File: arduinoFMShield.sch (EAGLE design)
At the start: 32 parts, among them IC1 ATMEGA168-MU, IC2 FT232RQ, X1 MINI-USB-32005-301, X2 R141426

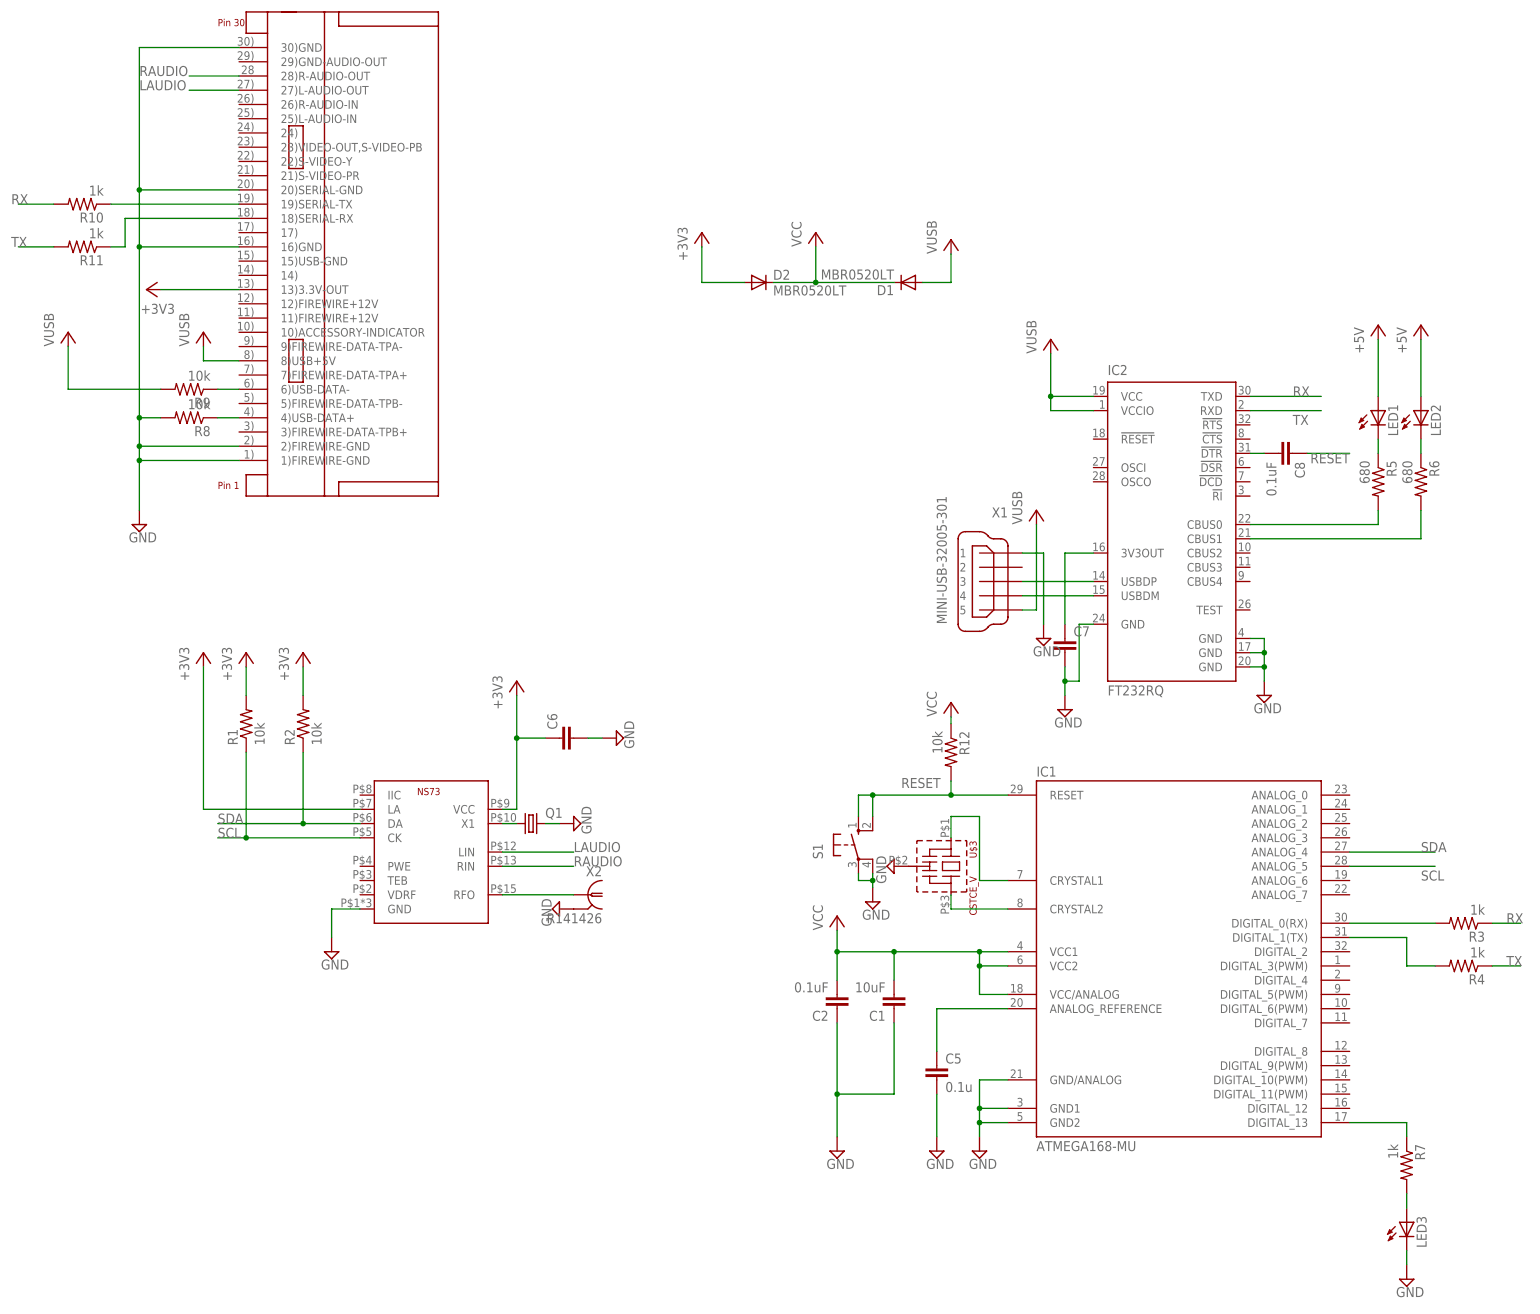
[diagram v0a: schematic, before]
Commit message: 8/31/2013 Changed FTDI chip and atmega to bigger package for easier soldering. Add murata resonator
Signed-off-by: goose1987 <phamh1987@gmail.com>
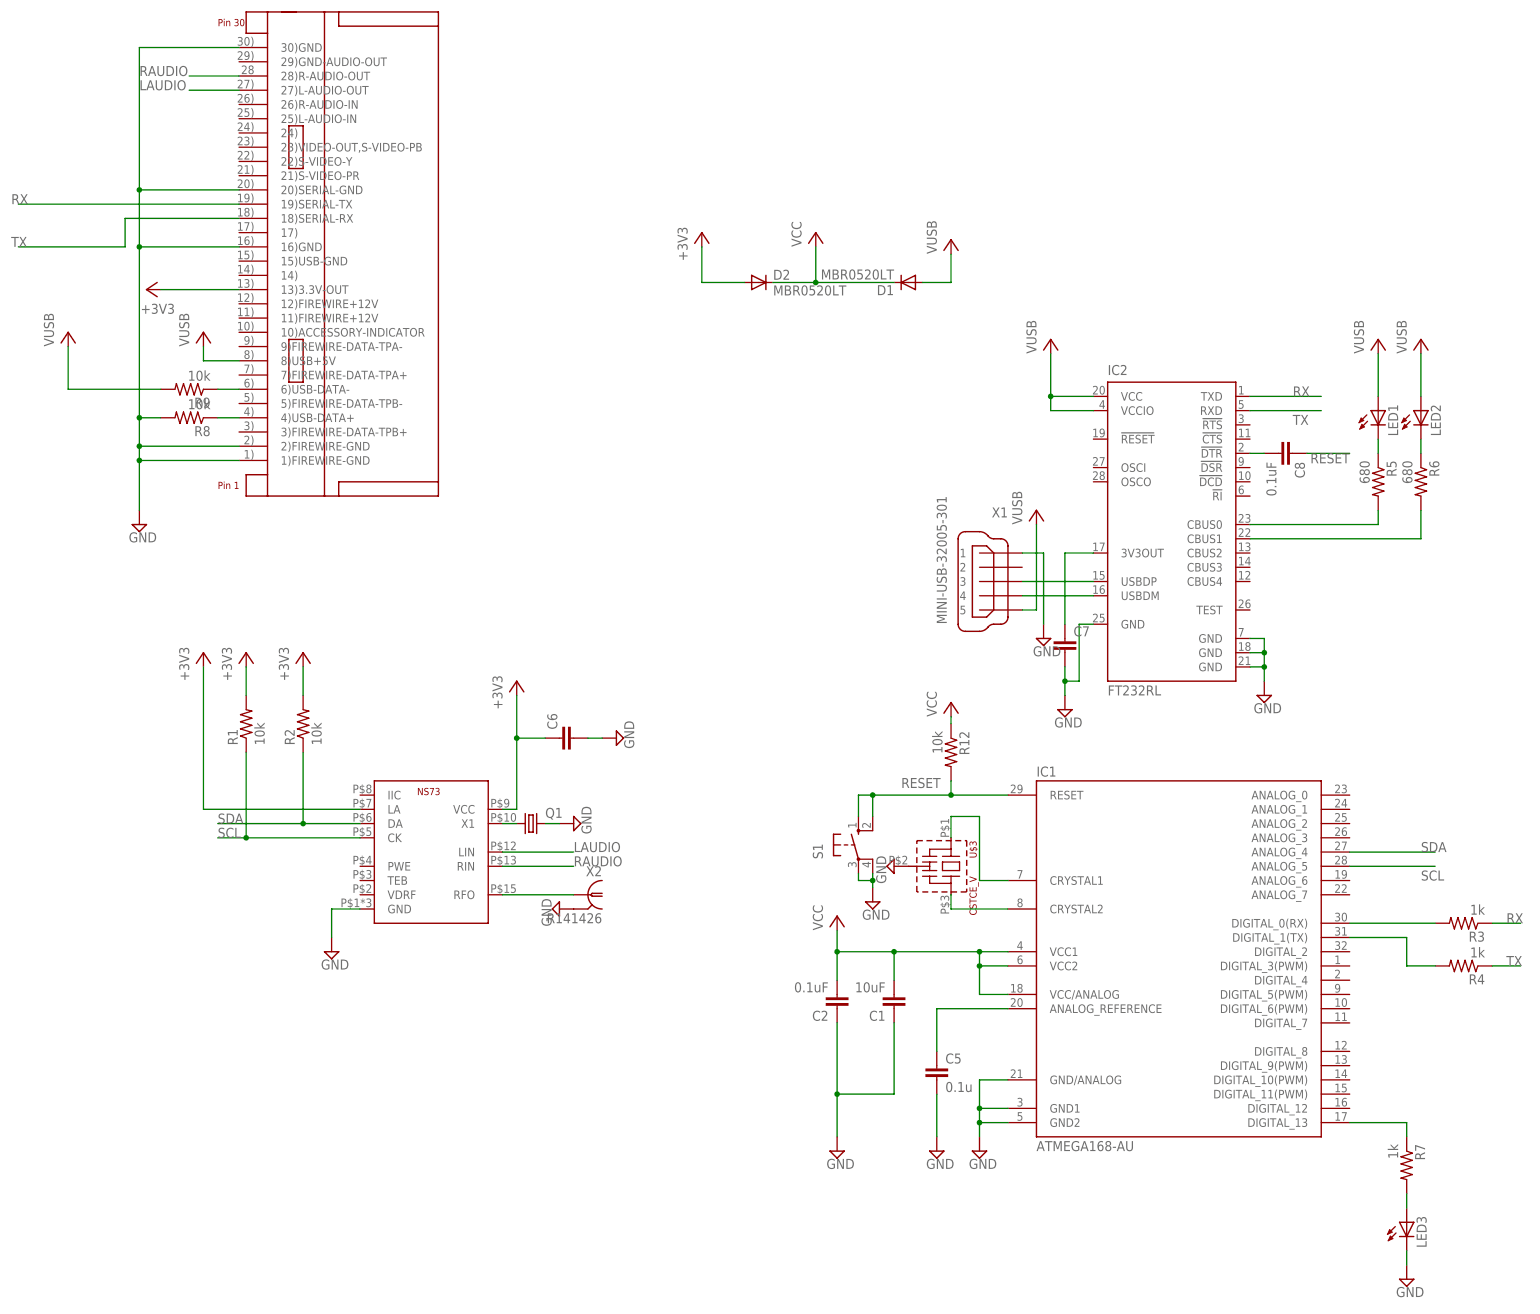
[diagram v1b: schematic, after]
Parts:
- removed R10, R11: 1k, rcl:R-US_R0805
- IC1: value ATMEGA168-MU -> ATMEGA168-AU; device Arduino-AVR:ATMEGA168-MU -> Arduino-AVR:ATMEGA168-AU
- IC2: value FT232RQ -> FT232RL; device ftdichip:FT232RQ -> ftdichip:FT232RL
- R12, R3, R4, R7: device rcl:R-US_R0805 -> rcl:R-US_R1206
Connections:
- removed net +5V: LED1.A, LED2.A
- removed net N$10: R11.1, U$2.18)SERIAL-RX
- removed net N$9: R10.1, U$2.19)SERIAL-TX
- net RX: now also U$2.19)SERIAL-TX; no longer R10.2
- net TX: now also U$2.18)SERIAL-RX; no longer R11.2
- net VUSB: now also LED1.A, LED2.A
